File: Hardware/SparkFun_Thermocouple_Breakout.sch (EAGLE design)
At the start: 15 parts, among them U1 MAX31855K

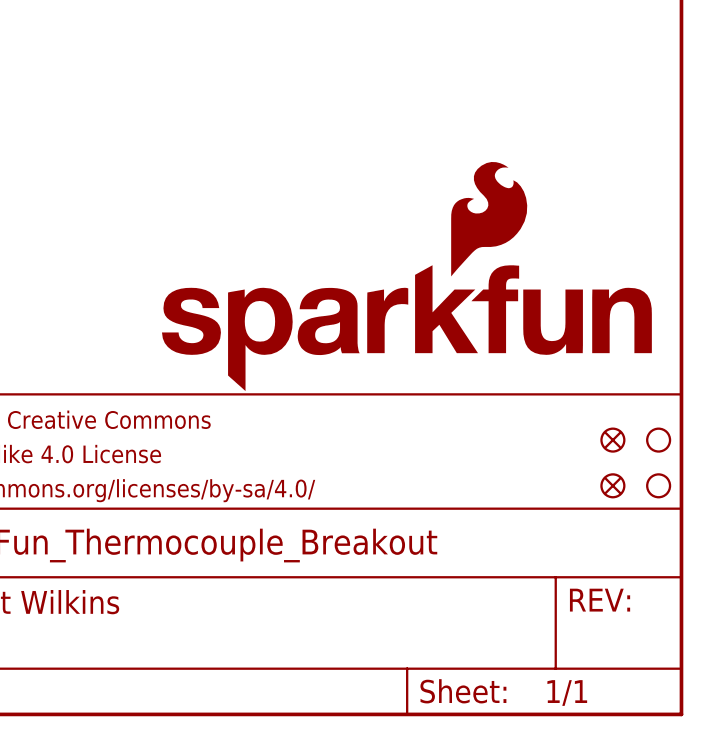
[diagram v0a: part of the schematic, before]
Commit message: Added a second logo to the back, mirrored the revision, & added the version number to the frame that disappeared with the new version of the frame
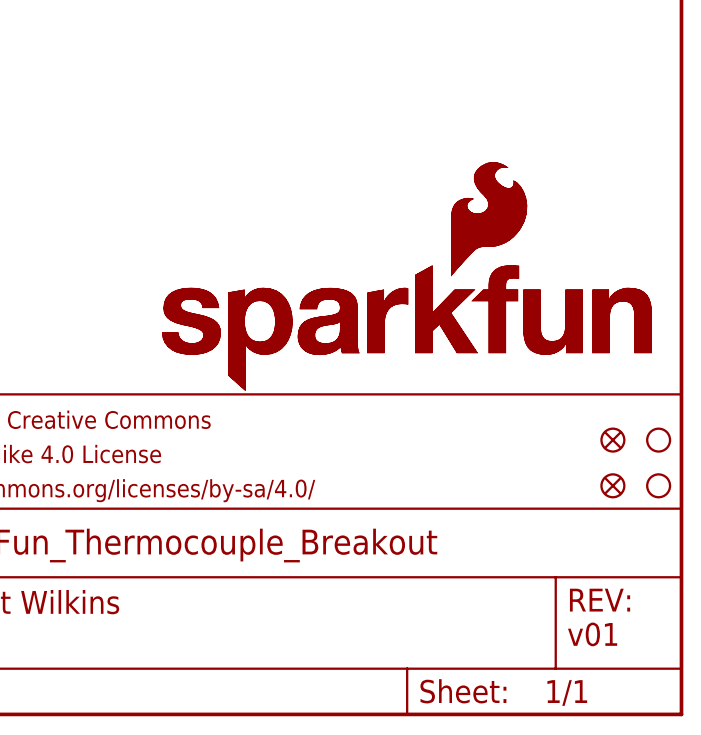
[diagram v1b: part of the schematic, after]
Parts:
- added LOGO3: SFE_LOGO_NAME_FLAME.1_INCH, SparkFun-Aesthetics:SFE_LOGO_NAME_FLAME.1_INCH
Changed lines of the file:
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@@
 <attributes>
 <attribute name="DESIGNER" value="Brent Wilkins"/>
+<attribute name="VERSION" value="v01"/>
 </attributes>
 <variantdefs>
@@
 <part name="C2" library="SparkFun-Capacitors" deviceset="10NF/10000PF-50V-10%(0603)" device="" value="10nF"/>
 <part name="JP2" library="Testing" deviceset="PCB_THERMOCOUPLE" device=""/>
+<part name="LOGO3" library="SparkFun-Aesthetics" deviceset="SFE_LOGO_NAME_FLAME" device=".1_INCH"/>
 </parts>
 <sheets>
 <sheet>
 <plain>
-<text x="165.862" y="11.176" size="2.54" layer="94">&gt;DESIGNER</text>
+<text x="165.862" y="11.176" size="2.54" layer="94" font="vector">&gt;DESIGNER</text>
+<text x="236.22" y="7.62" size="2.54" layer="94" font="vector">&gt;VERSION</text>
 </plain>
 <instances>
@@
 <attribute name="NAME" x="91.44" y="56.642" size="1.778" layer="95"/>
 </instance>
+<instance part="LOGO3" gate="G$1" x="190.5" y="35.56"/>
 </instances>
 <busses>

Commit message: Added more logos!
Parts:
- added LOGO4: OSHW-LOGOS, SparkFun-Aesthetics:OSHW-LOGOS
- U1: PROD_ID (none) -> IC-12578
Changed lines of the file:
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@@
 <part name="FID2" library="SparkFun-Aesthetics" deviceset="FIDUCIAL" device="1X2"/>
 <part name="C1" library="SparkFun-Capacitors" deviceset="0.1UF-25V(+80/-20%)(0603)" device="" value="0.1uF"/>
-<part name="U1" library="SparkFun-AnalogIC" deviceset="MAX31855K" device=""/>
+<part name="U1" library="SparkFun-AnalogIC" deviceset="MAX31855K" device="">
+<attribute name="PROD_ID" value="IC-12578"/>
+</part>
 <part name="GND2" library="SparkFun-Aesthetics" deviceset="GND" device=""/>
 <part name="JP1" library="SparkFun-Connectors" deviceset="M06" device="SILK_FEMALE_PTH" value="DNP"/>
@@
 <part name="JP2" library="Testing" deviceset="PCB_THERMOCOUPLE" device=""/>
 <part name="LOGO3" library="SparkFun-Aesthetics" deviceset="SFE_LOGO_NAME_FLAME" device=".1_INCH"/>
+<part name="LOGO4" library="SparkFun-Aesthetics" deviceset="OSHW-LOGO" device="S"/>
 </parts>
 <sheets>
@@
 <instance part="FID2" gate="G$1" x="241.3" y="25.4"/>
 <instance part="C1" gate="G$1" x="73.66" y="93.98" rot="MR0"/>
-<instance part="U1" gate="G$1" x="116.84" y="99.06"/>
+<instance part="U1" gate="G$1" x="116.84" y="99.06">
+<attribute name="PROD_ID" x="116.84" y="99.06" size="1.778" layer="96" display="off"/>
+</instance>
 <instance part="GND2" gate="1" x="73.66" y="86.36"/>
 <instance part="JP1" gate="G$1" x="162.56" y="96.52" rot="R180"/>
@@
 </instance>
 <instance part="LOGO3" gate="G$1" x="190.5" y="35.56"/>
+<instance part="LOGO4" gate="G$1" x="127" y="27.94"/>
 </instances>
 <busses>

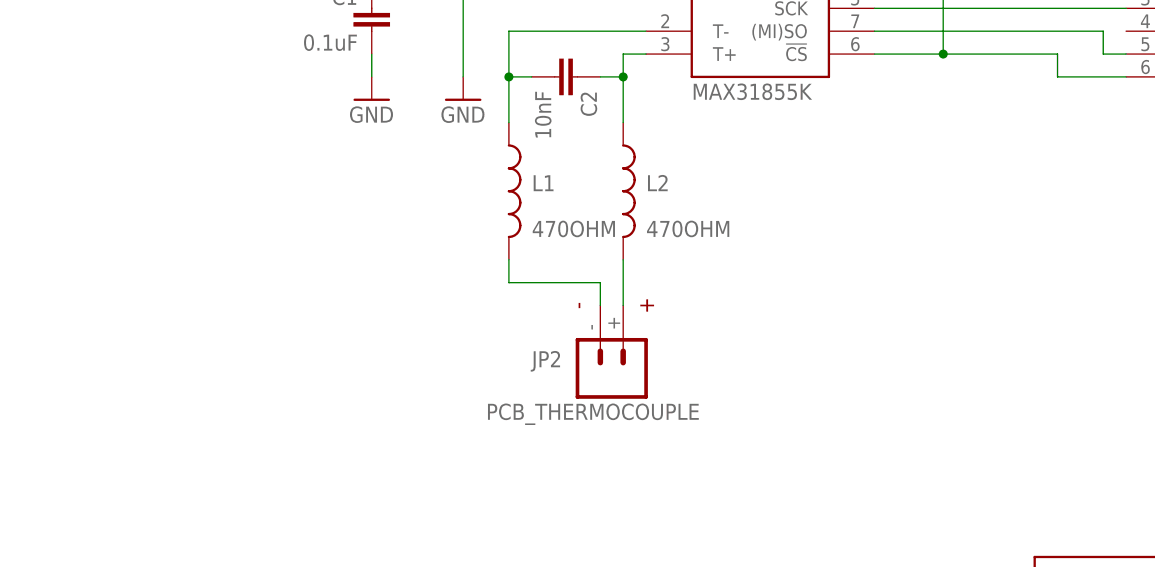
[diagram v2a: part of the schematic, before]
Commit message: Added testpoints for the thermocouple connections
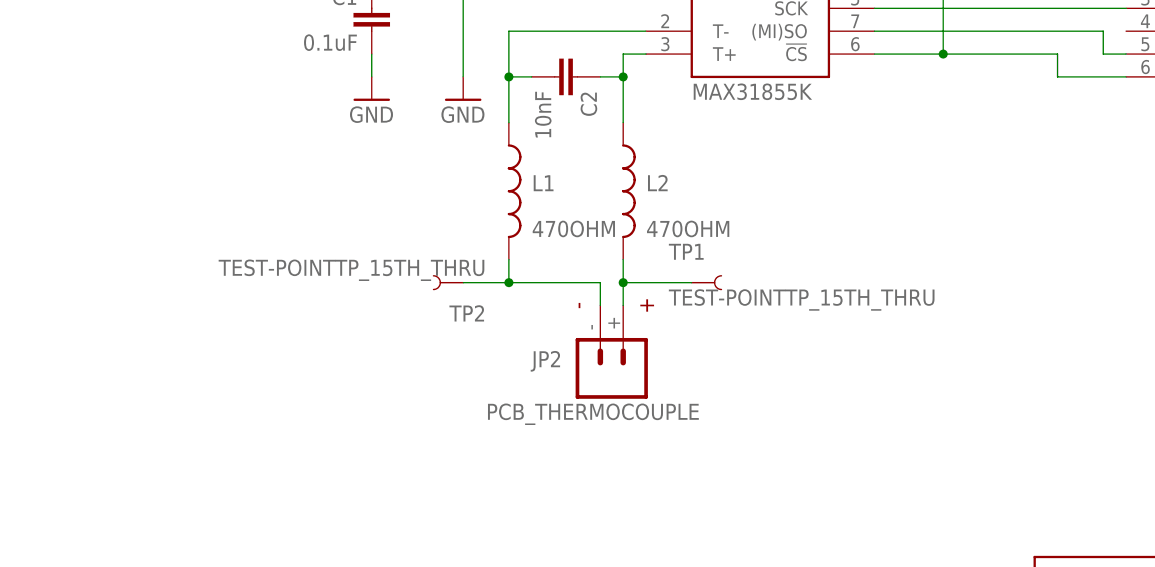
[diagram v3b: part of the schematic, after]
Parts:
- added TP1, TP2: TEST-POINTTP_15TH_THRU, SparkFun-Passives:TEST-POINTTP_15TH_THRU
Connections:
- net N$4: now also TP1.1
- net N$5: now also TP2.1
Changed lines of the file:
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@@
 <part name="LOGO3" library="SparkFun-Aesthetics" deviceset="SFE_LOGO_NAME_FLAME" device=".1_INCH"/>
 <part name="LOGO4" library="SparkFun-Aesthetics" deviceset="OSHW-LOGO" device="S"/>
+<part name="TP1" library="SparkFun-Passives" deviceset="TEST-POINT" device="TP_15TH_THRU"/>
+<part name="TP2" library="SparkFun-Passives" deviceset="TEST-POINT" device="TP_15TH_THRU"/>
 </parts>
 <sheets>
@@
 <instance part="LOGO3" gate="G$1" x="190.5" y="35.56"/>
 <instance part="LOGO4" gate="G$1" x="127" y="27.94"/>
+<instance part="TP1" gate="G$1" x="109.22" y="66.04"/>
+<instance part="TP2" gate="G$1" x="83.82" y="66.04" rot="R180"/>
 </instances>
 <busses>
@@
 <wire x1="99.06" y1="66.04" x2="99.06" y2="63.5" width="0.1524" layer="91"/>
 <pinref part="JP2" gate="G$1" pin="-"/>
+<pinref part="TP2" gate="G$1" pin="1"/>
+<wire x1="83.82" y1="66.04" x2="88.9" y2="66.04" width="0.1524" layer="91"/>
+<junction x="88.9" y="66.04"/>
 </segment>
 </net>
@@
 <segment>
 <pinref part="L2" gate="G$1" pin="2"/>
-<wire x1="101.6" y1="68.58" x2="101.6" y2="63.5" width="0.1524" layer="91"/>
+<wire x1="101.6" y1="68.58" x2="101.6" y2="66.04" width="0.1524" layer="91"/>
 <pinref part="JP2" gate="G$1" pin="+"/>
+<pinref part="TP1" gate="G$1" pin="1"/>
+<wire x1="101.6" y1="66.04" x2="101.6" y2="63.5" width="0.1524" layer="91"/>
+<wire x1="109.22" y1="66.04" x2="101.6" y2="66.04" width="0.1524" layer="91"/>
+<junction x="101.6" y="66.04"/>
 </segment>
 </net>
